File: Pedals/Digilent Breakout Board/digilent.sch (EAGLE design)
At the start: 5 parts

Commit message: Route board
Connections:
- net N$1 renamed SC1_P
- net N$2 renamed SC2_P
- net N$3 renamed SC1_N
- net N$4 renamed SC2_N
- net N$7 renamed WV_1
- removed net N$5: DIGILENT.9, WAVE_2.3, WAVE_2.4
- new net WV_2: DIGILENT.9, WAVE_2.1, WAVE_2.2
- net AGND: now also WAVE_2.3, WAVE_2.4; no longer WAVE_2.1, WAVE_2.2
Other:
- moved on the sheet: SCOPE_1, SCOPE_2, WAVE_1, WAVE_2

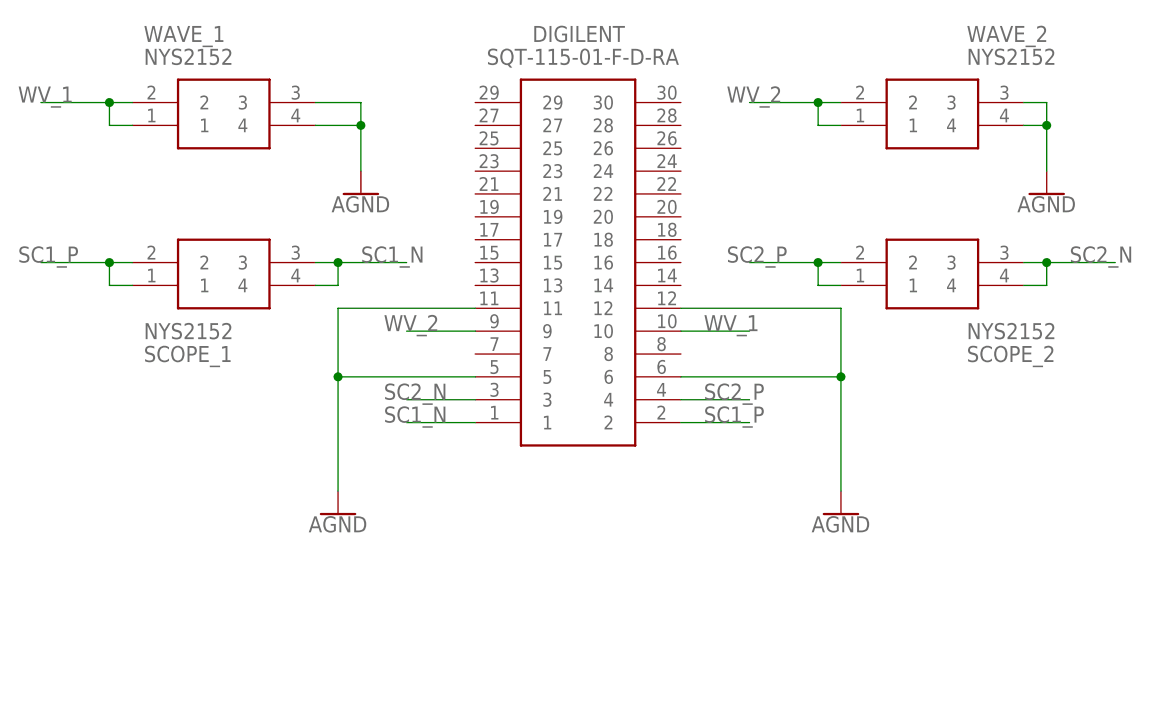
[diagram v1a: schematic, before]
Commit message: Put correct header on the digilent PCB
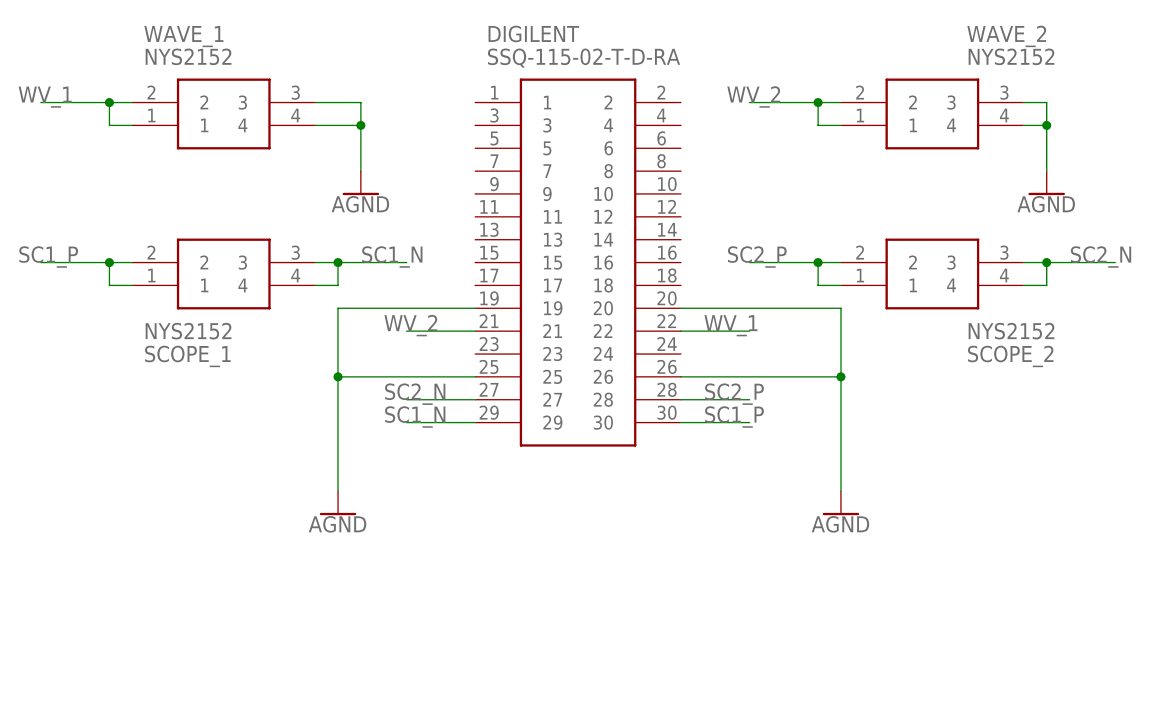
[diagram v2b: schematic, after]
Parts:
- DIGILENT: value SQT-115-01-F-D-RA -> SSQ-115-02-T-D-RA; device SamacSys_Parts:SQT-115-01-F-D-RA -> SamacSys_Parts:SSQ-115-02-T-D-RA
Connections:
- net AGND: now also DIGILENT.19, DIGILENT.20, DIGILENT.25, DIGILENT.26; no longer DIGILENT.11, DIGILENT.12, DIGILENT.5, DIGILENT.6
- net SC1_N: now also DIGILENT.29; no longer DIGILENT.1
- net SC1_P: now also DIGILENT.30; no longer DIGILENT.2
- net SC2_N: now also DIGILENT.27; no longer DIGILENT.3
- net SC2_P: now also DIGILENT.28; no longer DIGILENT.4
- net WV_1: now also DIGILENT.22; no longer DIGILENT.10
- net WV_2: now also DIGILENT.21; no longer DIGILENT.9
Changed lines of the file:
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@@
 </classes>
 <parts>
-<part name="DIGILENT" library="SamacSys_Parts" deviceset="SQT-115-01-F-D-RA" device=""/>
 <part name="SCOPE_1" library="SamacSys_Parts" deviceset="NYS2152" device=""/>
 <part name="SCOPE_2" library="SamacSys_Parts" deviceset="NYS2152" device=""/>
@@
 <part name="U$3" library="SparkFun-PowerSymbols" library_urn="urn:adsk.eagle:library:530" deviceset="AGND" device=""/>
 <part name="U$4" library="SparkFun-PowerSymbols" library_urn="urn:adsk.eagle:library:530" deviceset="AGND" device=""/>
+<part name="DIGILENT" library="SamacSys_Parts" deviceset="SSQ-115-02-T-D-RA" device=""/>
 </parts>
 <sheets>
@@
 </plain>
 <instances>
-<instance part="DIGILENT" gate="G$1" x="58.42" y="68.58" smashed="yes">
-<attribute name="NAME" x="64.77" y="76.2" size="1.778" layer="95" align="center-left"/>
-<attribute name="VALUE" x="59.69" y="73.66" size="1.778" layer="96" align="center-left"/>
-</instance>
 <instance part="SCOPE_1" gate="G$1" x="20.32" y="50.8" smashed="yes">
 <attribute name="NAME" x="21.59" y="40.64" size="1.778" layer="95" align="center-left"/>
@@
 <attribute name="VALUE" x="45.72" y="58.166" size="1.778" layer="96" align="top-center"/>
 </instance>
+<instance part="DIGILENT" gate="G$1" x="58.42" y="68.58" smashed="yes">
+<attribute name="NAME" x="59.69" y="76.2" size="1.778" layer="95" align="center-left"/>
+<attribute name="VALUE" x="59.69" y="73.66" size="1.778" layer="96" align="center-left"/>
+</instance>
 </instances>
 <busses>
@@
 <net name="AGND" class="0">
 <segment>
-<pinref part="DIGILENT" gate="G$1" pin="6"/>
 <wire x1="81.28" y1="38.1" x2="99.06" y2="38.1" width="0.1524" layer="91"/>
 <wire x1="99.06" y1="38.1" x2="99.06" y2="25.4" width="0.1524" layer="91"/>
 <pinref part="U$1" gate="G$1" pin="AGND"/>
-<pinref part="DIGILENT" gate="G$1" pin="12"/>
 <wire x1="81.28" y1="45.72" x2="99.06" y2="45.72" width="0.1524" layer="91"/>
 <wire x1="99.06" y1="45.72" x2="99.06" y2="38.1" width="0.1524" layer="91"/>
 <junction x="99.06" y="38.1"/>
+<pinref part="DIGILENT" gate="G$1" pin="20"/>
+<pinref part="DIGILENT" gate="G$1" pin="26"/>
 </segment>
 <segment>
-<pinref part="DIGILENT" gate="G$1" pin="5"/>
 <wire x1="58.42" y1="38.1" x2="43.18" y2="38.1" width="0.1524" layer="91"/>
 <pinref part="U$2" gate="G$1" pin="AGND"/>
 <wire x1="43.18" y1="38.1" x2="43.18" y2="25.4" width="0.1524" layer="91"/>
-<pinref part="DIGILENT" gate="G$1" pin="11"/>
 <wire x1="58.42" y1="45.72" x2="43.18" y2="45.72" width="0.1524" layer="91"/>
 <wire x1="43.18" y1="45.72" x2="43.18" y2="38.1" width="0.1524" layer="91"/>
 <junction x="43.18" y="38.1"/>
+<pinref part="DIGILENT" gate="G$1" pin="19"/>
+<pinref part="DIGILENT" gate="G$1" pin="25"/>
 </segment>
 <segment>
@@
 <net name="SC1_N" class="0">
 <segment>
-<pinref part="DIGILENT" gate="G$1" pin="1"/>
 <wire x1="58.42" y1="33.02" x2="50.8" y2="33.02" width="0.1524" layer="91"/>
 <label x="48.26" y="33.02" size="1.778" layer="95"/>
+<pinref part="DIGILENT" gate="G$1" pin="29"/>
 </segment>
 <segment>
@@
 <net name="SC2_N" class="0">
 <segment>
-<pinref part="DIGILENT" gate="G$1" pin="3"/>
 <wire x1="58.42" y1="35.56" x2="50.8" y2="35.56" width="0.1524" layer="91"/>
 <label x="48.26" y="35.56" size="1.778" layer="95"/>
+<pinref part="DIGILENT" gate="G$1" pin="27"/>
 </segment>
 <segment>
@@
 <net name="SC2_P" class="0">
 <segment>
-<pinref part="DIGILENT" gate="G$1" pin="4"/>
 <wire x1="81.28" y1="35.56" x2="88.9" y2="35.56" width="0.1524" layer="91"/>
 <label x="83.82" y="35.56" size="1.778" layer="95"/>
+<pinref part="DIGILENT" gate="G$1" pin="28"/>
 </segment>
 <segment>
@@
 <net name="SC1_P" class="0">
 <segment>
-<pinref part="DIGILENT" gate="G$1" pin="2"/>
 <wire x1="81.28" y1="33.02" x2="88.9" y2="33.02" width="0.1524" layer="91"/>
 <label x="83.82" y="33.02" size="1.778" layer="95"/>
+<pinref part="DIGILENT" gate="G$1" pin="30"/>
 </segment>
 <segment>
@@
 <net name="WV_1" class="0">
 <segment>
-<pinref part="DIGILENT" gate="G$1" pin="10"/>
 <wire x1="81.28" y1="43.18" x2="88.9" y2="43.18" width="0.1524" layer="91"/>
 <label x="83.82" y="43.18" size="1.778" layer="95"/>
+<pinref part="DIGILENT" gate="G$1" pin="22"/>
 </segment>
 <segment>
@@
 <net name="WV_2" class="0">
 <segment>
-<pinref part="DIGILENT" gate="G$1" pin="9"/>
 <wire x1="58.42" y1="43.18" x2="50.8" y2="43.18" width="0.1524" layer="91"/>
 <label x="48.26" y="43.18" size="1.778" layer="95"/>
+<pinref part="DIGILENT" gate="G$1" pin="21"/>
 </segment>
 <segment>
